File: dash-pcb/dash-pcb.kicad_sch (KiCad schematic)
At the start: 17 parts, among them U2 Teensy2.0_(Arduino)

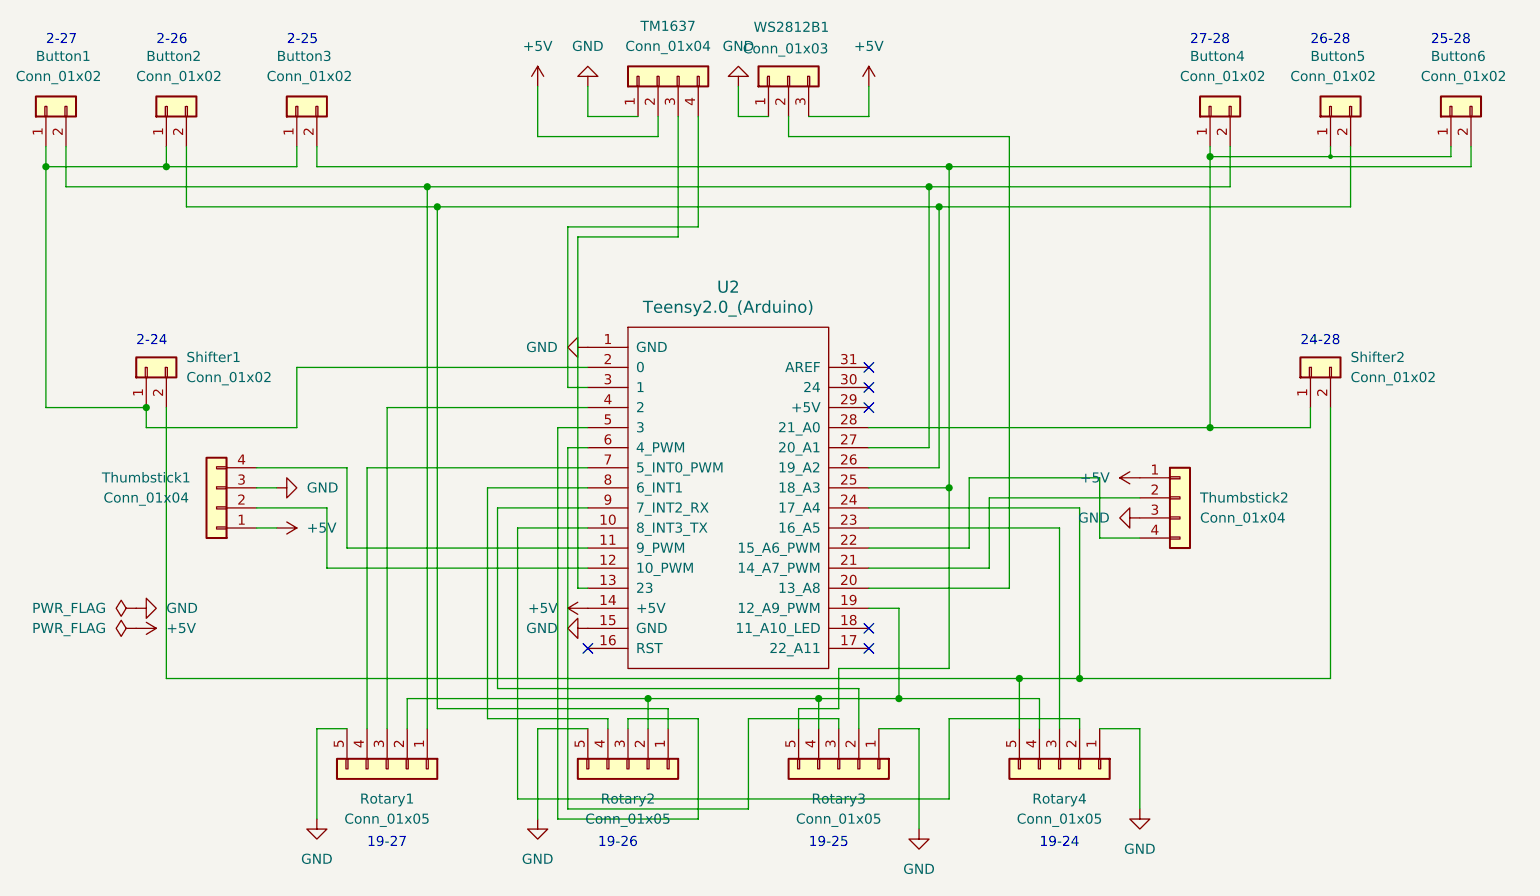
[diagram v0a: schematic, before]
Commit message: fixed thumbstick 1 analogic pin
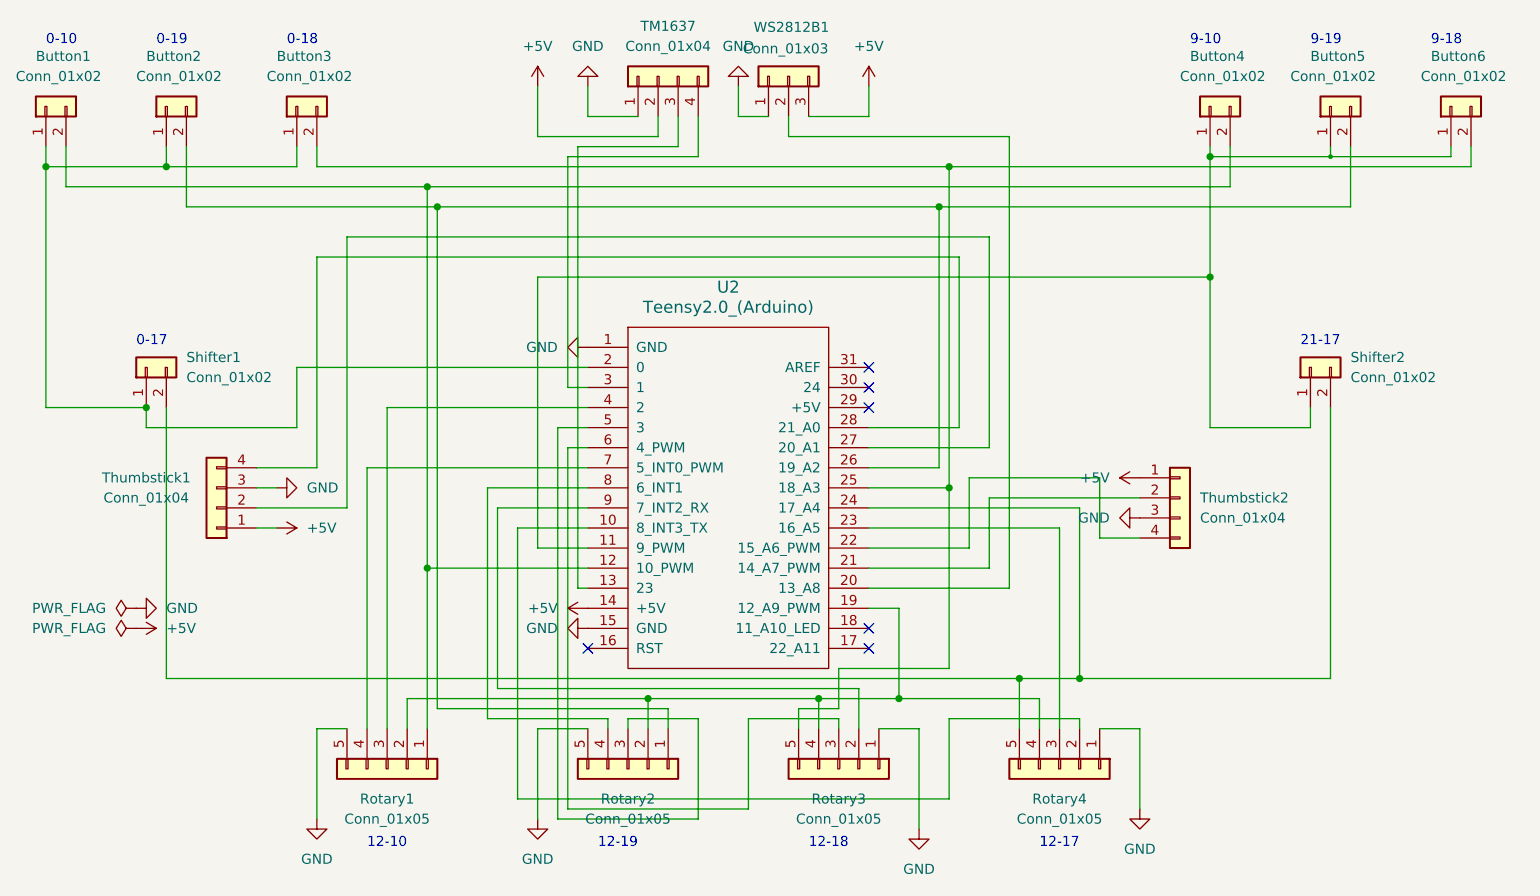
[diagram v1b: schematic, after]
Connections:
- net at Button1.2 (Pin_2), Button4.2 (Pin_2), Rotary1.1 (Pin_1): now also U2.12 (10_PWM); no longer U2.27 (20_A1)
- net at U2.11 (9_PWM): now also Button4.1 (Pin_1), Button5.1 (Pin_1), Button6.1 (Pin_1), Shifter2.1 (Pin_1); no longer Thumbstick1.4 (Pin_4)
- net at Thumbstick1.2 (Pin_2): now also U2.27 (20_A1); no longer U2.12 (10_PWM)
- new net: Thumbstick1.4 (Pin_4), U2.28 (21_A0)
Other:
- note added: "0-10"
- note added: "0-17"
- note added: "0-18"
- note added: "0-19"
- note added: "12-10"
- note added: "12-17"
- note added: "12-18"
- note added: "12-19"
- note added: "21-17"
- note added: "9-10"
- note added: "9-18"
- note added: "9-19"
- note removed: "19-24"
- note removed: "19-25"
- note removed: "19-26"
- note removed: "19-27"
- note removed: "2-24"
- note removed: "2-25"
- note removed: "2-26"
- note removed: "2-27"
- note removed: "24-28"
- note removed: "25-28"
- note removed: "26-28"
- note removed: "27-28"
